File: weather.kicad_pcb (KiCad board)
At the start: 2 copper layers, 24.1 x 24.1 mm, 23 parts, among them J1 Tag-Connect, U1 nRF52810-QCxx, U2 HDC2080, Y1 32MHz, Y2 32kHz

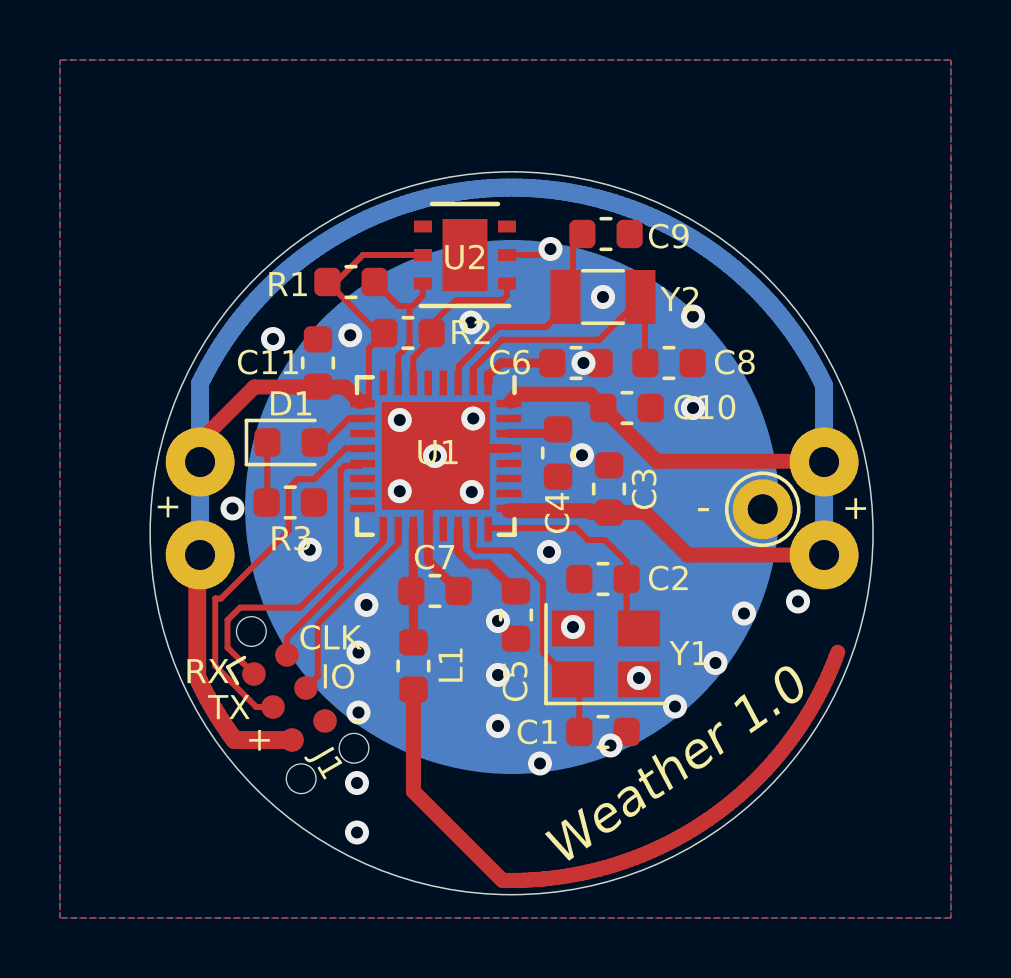
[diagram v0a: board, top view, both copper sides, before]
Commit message: Move LED to analog pin
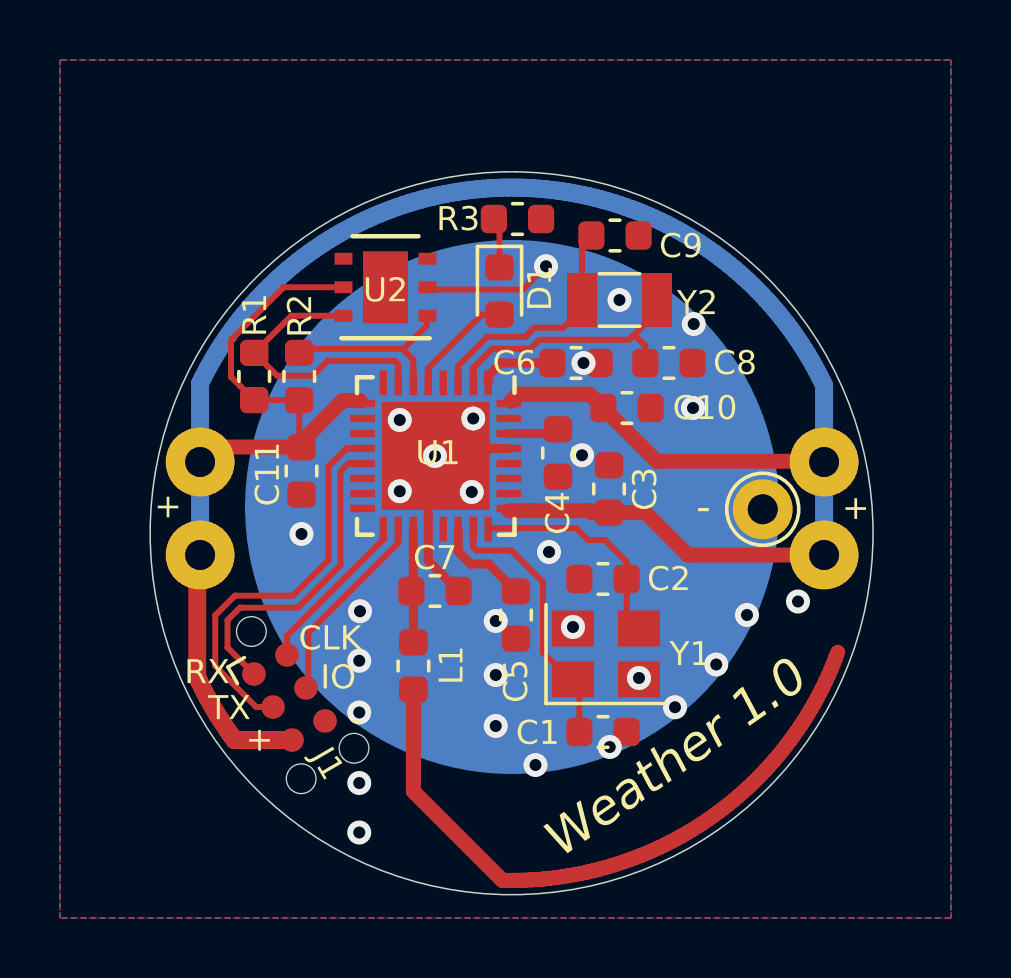
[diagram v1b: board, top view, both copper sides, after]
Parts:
- moved R3 12.1 mm to (112.3, 66.6)
- moved D1 8.59 mm to (111.8, 69.0), turned to 270 degrees
- moved R1 4.51 mm to (103.6, 71.8), turned to 90 degrees
- moved R2 3.90 mm to (105.1, 71.8), turned to 90 degrees
- moved C11 3.64 mm to (105.2, 75.0), turned to 270 degrees
- moved U2 2.86 mm to (108.0, 68.9)
- moved Y2 0.56 mm to (115.8, 69.3)
- moved C9 0.30 mm to (115.6, 67.2)
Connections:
- U1 pad 10: Net-(D1-Pad2) -> Net-(U1-Pad10)
- U1 pad 5: Net-(U1-Pad5) -> Net-(D1-Pad2)
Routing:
- net /SCL: track 5.21 -> 9.47 mm
- net GNDREF: track 9.16 -> 11.9 mm, vias 33 -> 29
- net Net-(D1-Pad2): track 1.93 -> 3.85 mm
- net /SDA: track 5.51 -> 6.33 mm
- net /TX: track 12.6 -> 13.2 mm
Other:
- rule pad_to_mask_clearance: 0.05 -> 0

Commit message: HDC2080 DRDY / INT pin, and move LED pin
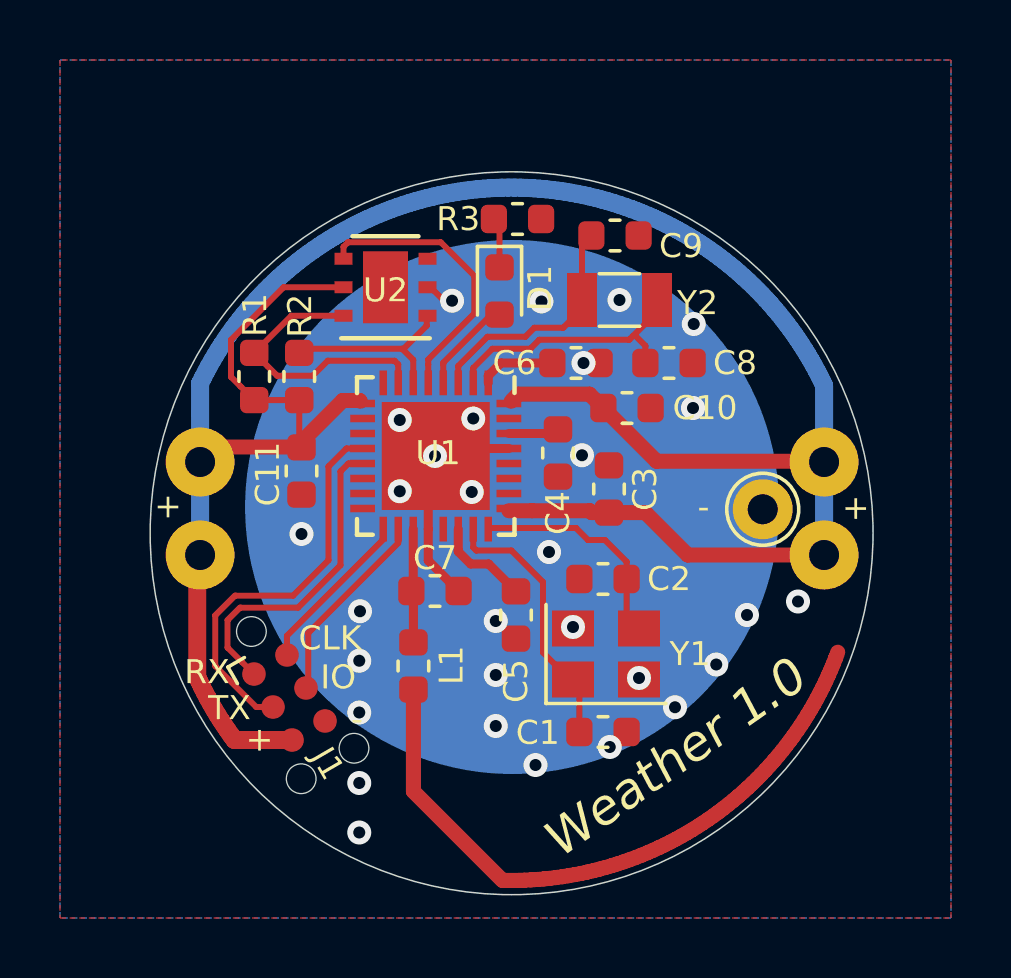
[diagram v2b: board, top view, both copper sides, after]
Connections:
- U1 pad 4: Net-(U1-Pad4) -> Net-(D1-Pad2)
- U1 pad 5: Net-(D1-Pad2) -> /DRDY
- U2 pad 4: Net-(U2-Pad4) -> /DRDY
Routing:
- net /DRDY: track 0.00 -> 9.49 mm
- net GNDREF: track 11.9 -> 8.63 mm, vias 29 -> 30
- net Net-(D1-Pad2): track 3.85 -> 3.21 mm

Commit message: KiCad upgrade
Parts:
- moved U2 0.06 mm to (107.9, 68.9)
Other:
- board text added: "Weather 1.1"
- board text removed: "Weather 1.0"

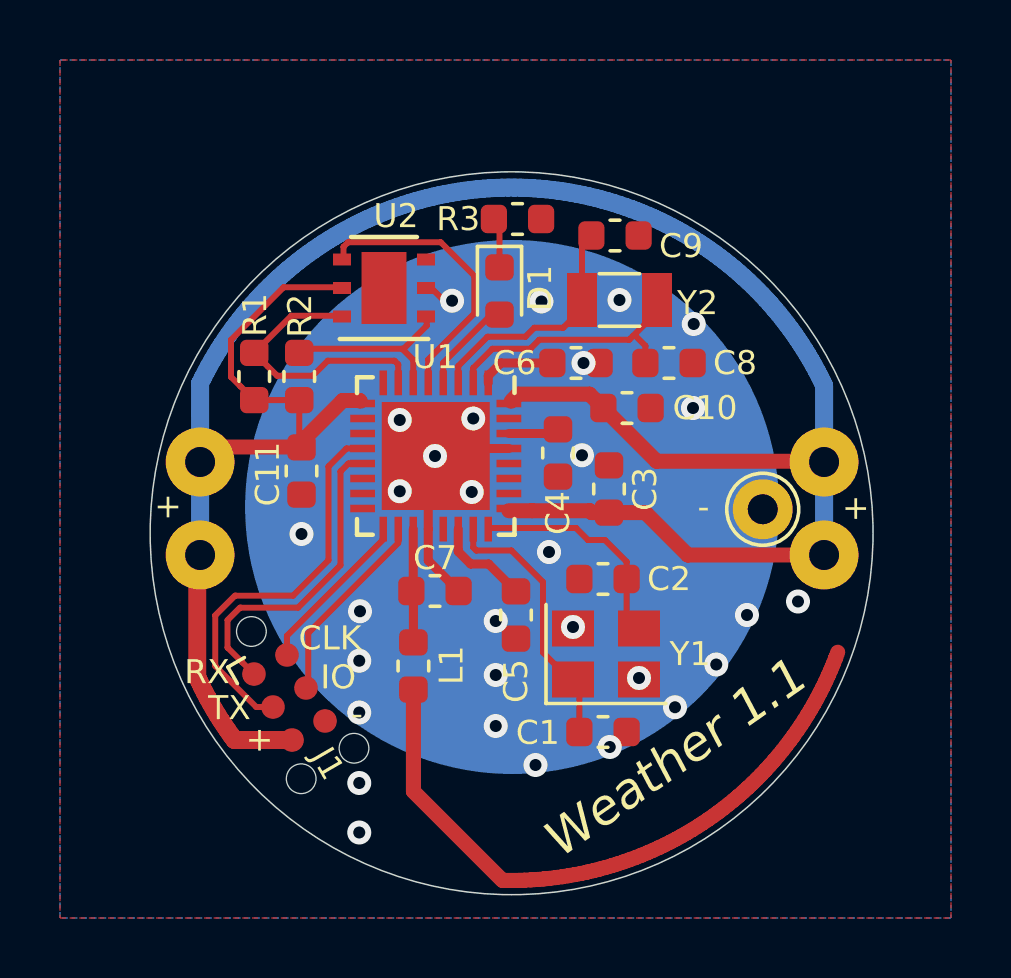
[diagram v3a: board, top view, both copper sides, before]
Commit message: Switch to BME680 sensor
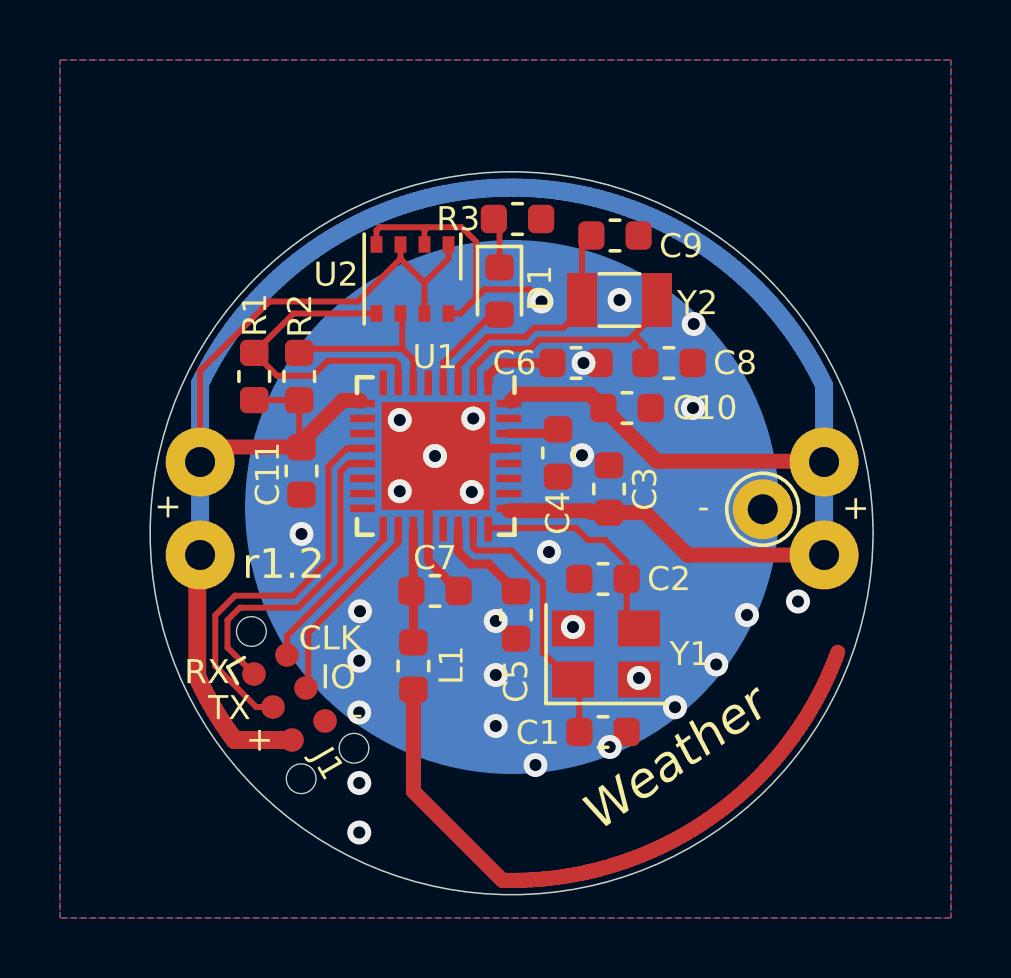
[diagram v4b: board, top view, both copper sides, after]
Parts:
- U2: value HDC2080 -> BME680; footprint Package_SON:Texas_PWSON-N6 -> Package_LGA:Bosch_LGA-8_3x3mm_P0.8mm_ClockwisePinNumbering
- moved U2 1.00 mm to (108.8, 68.6)
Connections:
- net Net-(AE1-Pad1) renamed /ANTENNA
- U1 pad 5: /DRDY -> Net-(U1-Pad5)
- U2 pad 1: /SDA -> GNDREF
- U2 pad 2: GNDREF -> +BATT
- U2 pad 3: Net-(U2-Pad3) -> /SDA
- U2 pad 4: /DRDY -> /SCL
- U2 pad 5: +BATT -> GNDREF
- U2 pad 6: /SCL -> +BATT
- U2 pad 7: Net-(U2-Pad7) -> GNDREF
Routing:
- net /DRDY: track 9.49 -> 0.00 mm
- net GNDREF: track 8.63 -> 17.7 mm, vias 30 -> 29
- net +BATT: track 84.7 -> 93.4 mm
- net /SCL: track 9.47 -> 10.6 mm
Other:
- board text added: "Weather"
- board text added: "r1.2"
- board text removed: "Weather 1.1"
